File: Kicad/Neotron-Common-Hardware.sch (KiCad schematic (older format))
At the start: 17 parts, among them J101 Neotron-Expansion-Slot, J102 Neotron-Expansion-Slot, J103 Neotron-Expansion-Slot, J104 Neotron-Expansion-Slot, U101 Neotron-CPU

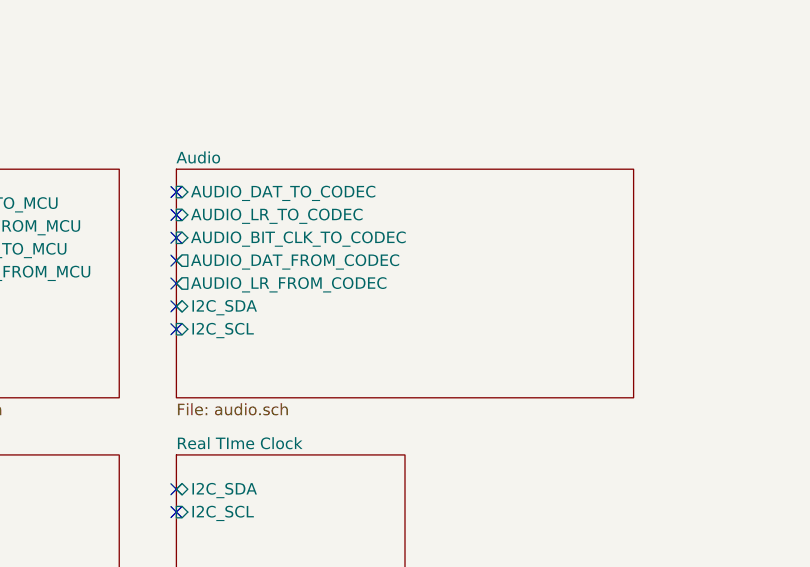
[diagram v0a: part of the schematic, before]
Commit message: Switch some of the radial THT Electrolytic caps for SMD MLCCs.
Also changed the STM32 for an LQFP-32 as it has a bigger pitch on the
pins.

The LQFP is easier to solder than the TSSOP, and the MLCC takes are
cheaper and take up less space.
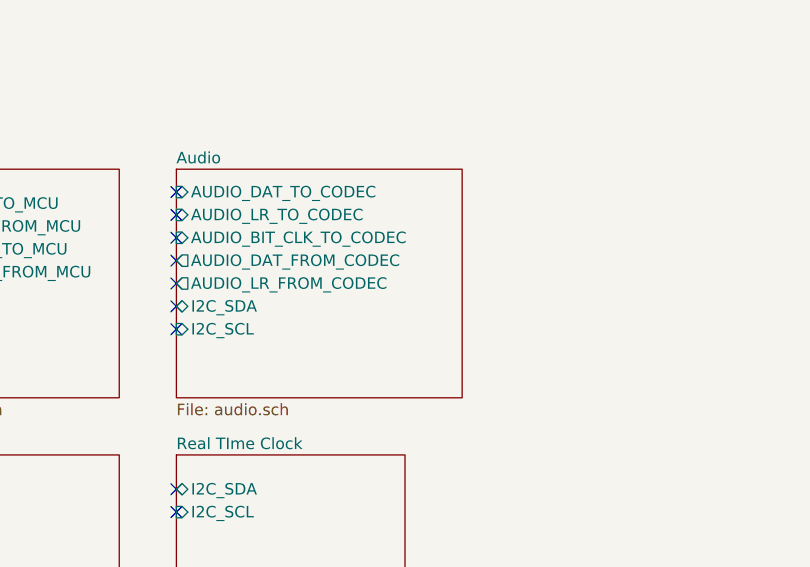
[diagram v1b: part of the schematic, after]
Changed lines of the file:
@@
 $EndSheet
 $Sheet
-S 8250 1500 2000 1000
+S 8250 1500 1250 1000
 U 5FDE6C5A
 F0 "Audio" 50

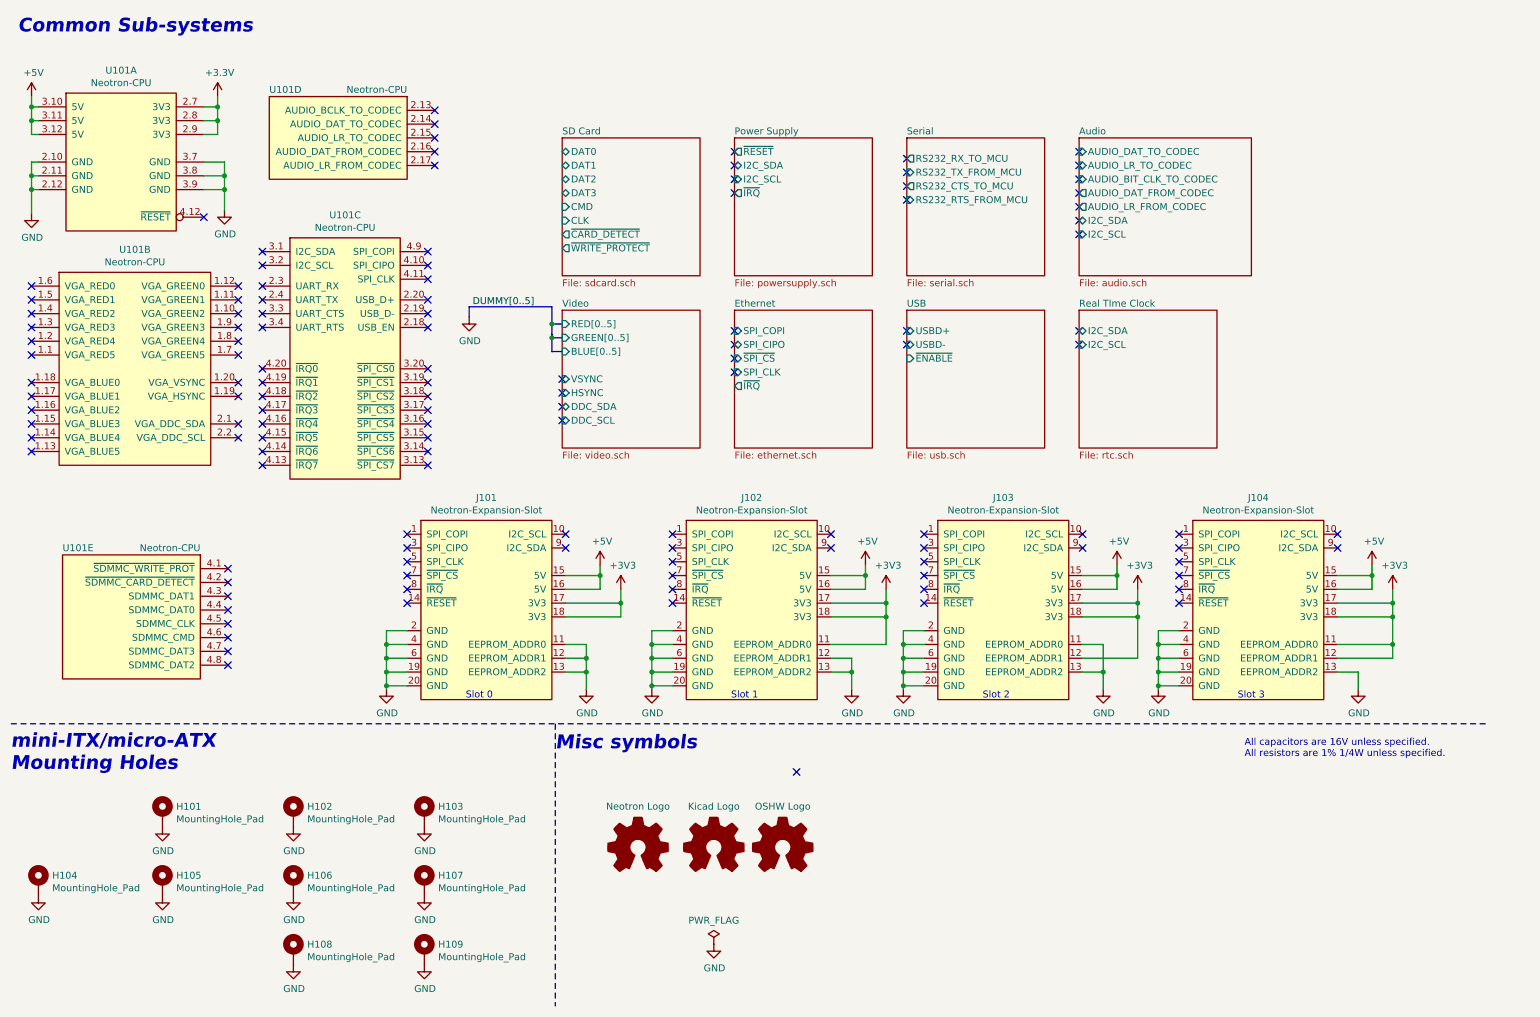
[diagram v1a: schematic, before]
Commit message: Added 12-bit video DAC.
Also had to change footprints to suit Kicad 5.1.9
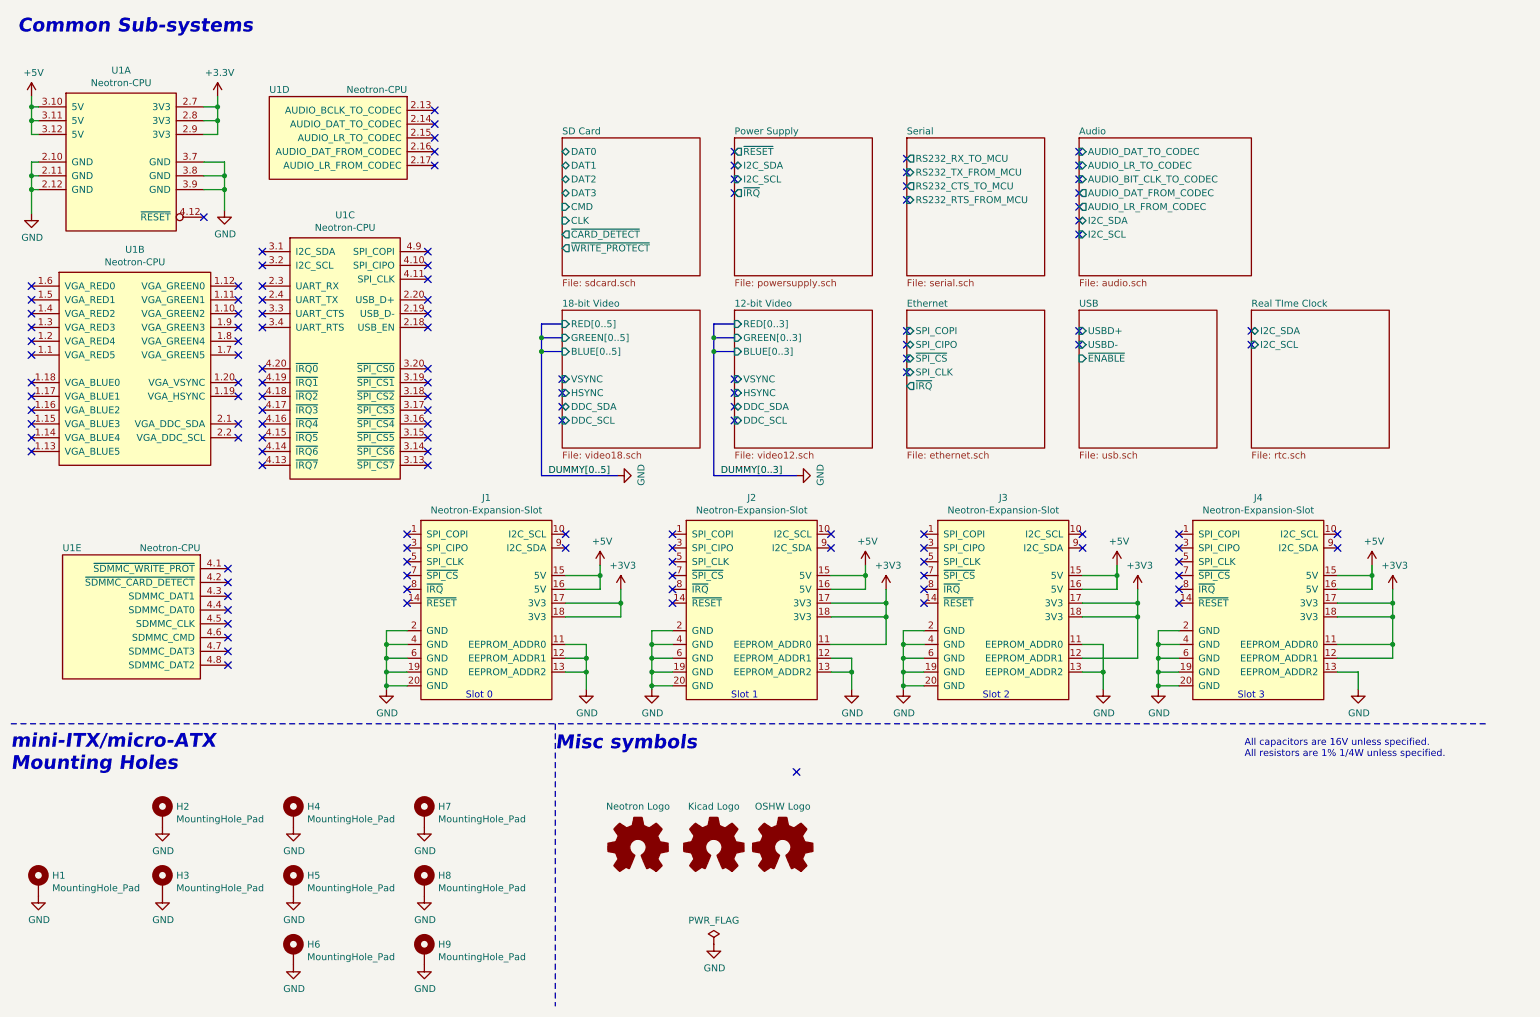
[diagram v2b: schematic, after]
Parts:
- renumbered H104 to H1, H101 to H2, H105 to H3, H102 to H4, H106 to H5, H108 to H6, H103 to H7, H107 to H8, H109 to H9, J101 to J1, J102 to J2, J103 to J3, J104 to J4, LOGO101 to LOGO1, LOGO102 to LOGO2, LOGO103 to LOGO3, U101 to U1
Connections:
- no-connect marks 124 -> 128

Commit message: Add 4-bit Video DAC, and re-wire BMC.
Now the BMC is an SPI device, and has a four-wire UART.
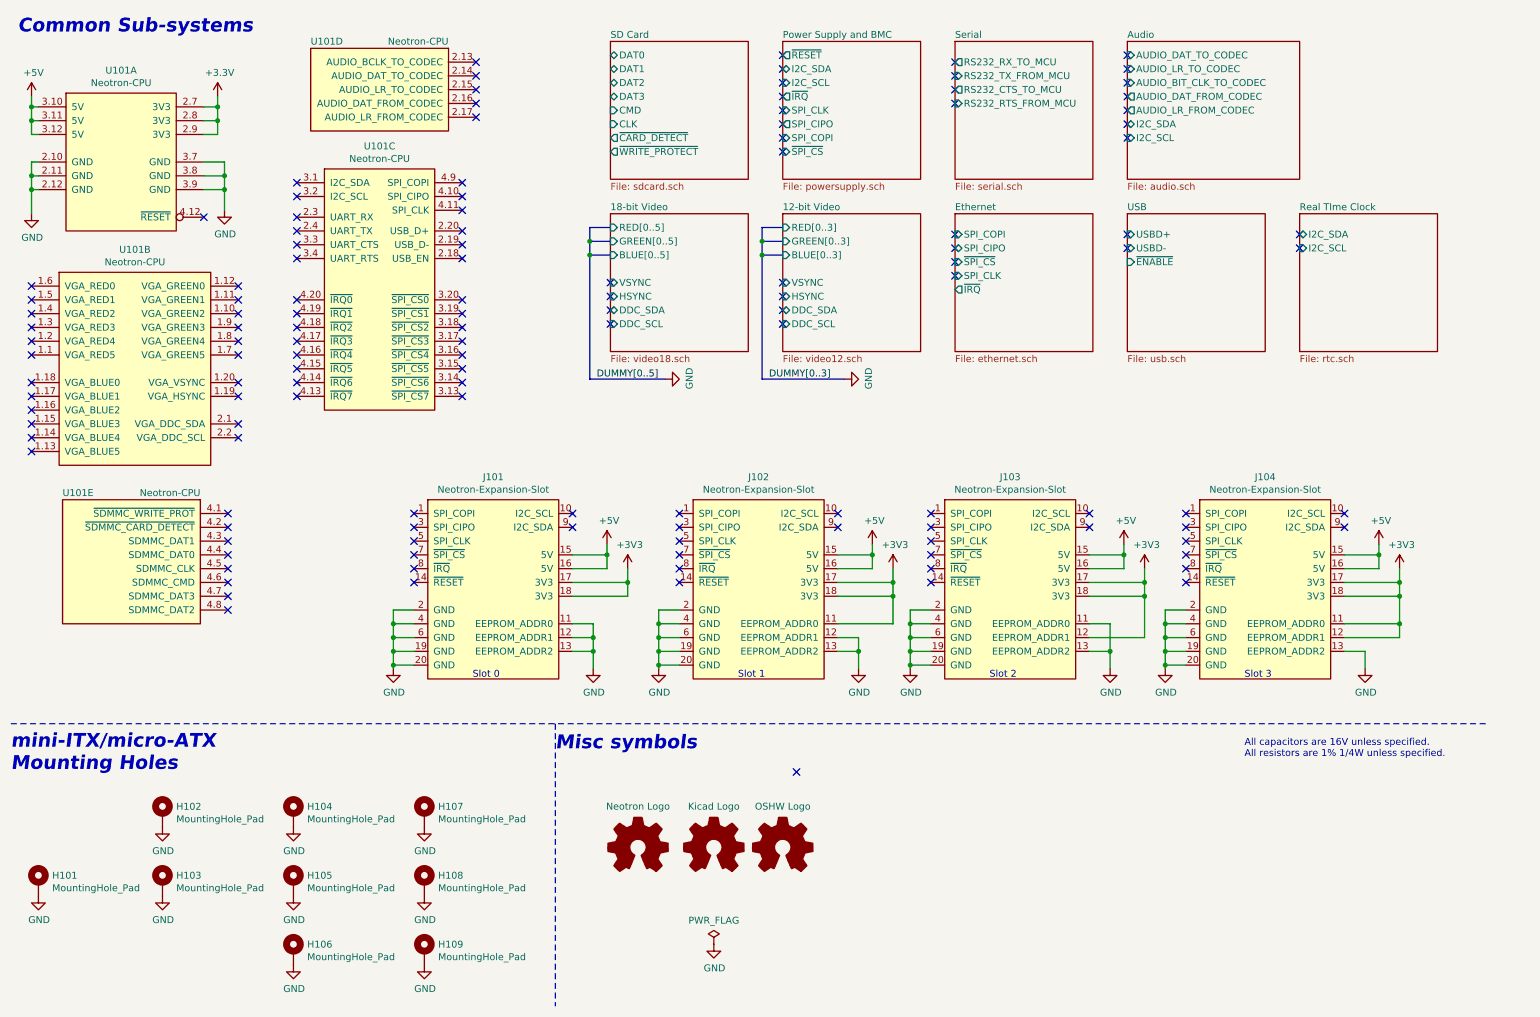
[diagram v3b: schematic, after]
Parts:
- renumbered H1 to H101, H2 to H102, H3 to H103, H4 to H104, H5 to H105, H6 to H106, H7 to H107, H8 to H108, H9 to H109, J1 to J101, J2 to J102, J3 to J103, J4 to J104, LOGO1 to LOGO101, LOGO2 to LOGO102, LOGO3 to LOGO103, U1 to U101
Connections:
- no-connect marks 128 -> 132
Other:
- moved on the sheet: J101, J102, J103, J104, U101C, U101D, U101E

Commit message: Tidy up part nos and swapped I2C/UART on BMC.
Mark all resistors as 1% if not specified.
Added some Mouser part numbers.
BMC can now be programmed over UART.
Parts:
- J101, J102, J103, J104: Mouser (none) -> 571-5-5530843-0
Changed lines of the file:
@@
 F 6 "5-5530843-0" H 4025 4675 50  0001 C CNN "MPN"
 F 7 "TE" H 4025 4675 50  0001 C CNN "Manufacturer"
+F 8 "571-5-5530843-0" H 4025 4675 50  0001 C CNN "Mouser"
 	1    4025 4675
 	1    0    0    -1
@@
 F 6 "5-5530843-0" H 5950 4675 50  0001 C CNN "MPN"
 F 7 "TE" H 5950 4675 50  0001 C CNN "Manufacturer"
+F 8 "571-5-5530843-0" H 5950 4675 50  0001 C CNN "Mouser"
 	1    5950 4675
 	1    0    0    -1
@@
 F 6 "5-5530843-0" H 7775 4675 50  0001 C CNN "MPN"
 F 7 "TE" H 7775 4675 50  0001 C CNN "Manufacturer"
+F 8 "571-5-5530843-0" H 7775 4675 50  0001 C CNN "Mouser"
 	1    7775 4675
 	1    0    0    -1
@@
 F 6 "5-5530843-0" H 9625 4675 50  0001 C CNN "MPN"
 F 7 "TE" H 9625 4675 50  0001 C CNN "Manufacturer"
+F 8 "571-5-5530843-0" H 9625 4675 50  0001 C CNN "Mouser"
 	1    9625 4675
 	1    0    0    -1
